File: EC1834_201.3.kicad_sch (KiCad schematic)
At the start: 64 parts

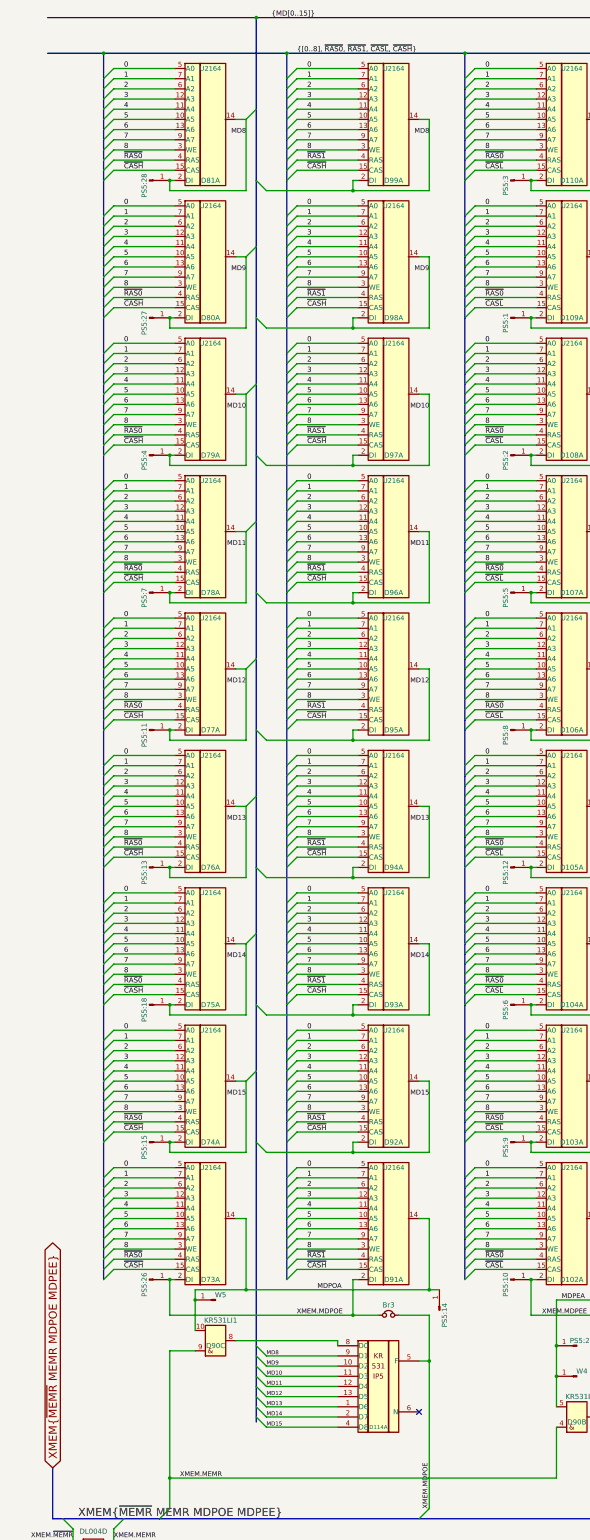
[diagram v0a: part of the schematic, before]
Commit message: Improved schematics and docs
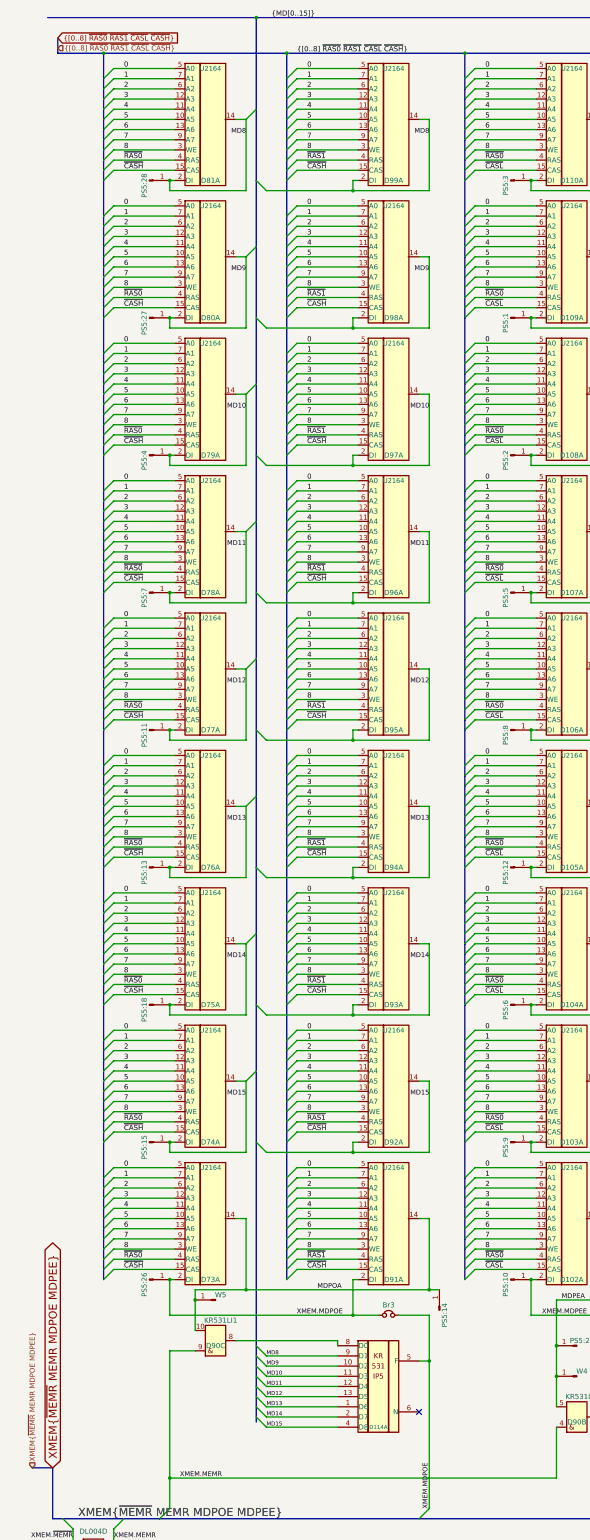
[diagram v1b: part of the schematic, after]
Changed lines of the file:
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@@
     (date "2022-09-05")
   )
+  (bus_alias "XMEM" (members ))
   (junction (at 144.78 231.14) (diameter 0) (color 0 0 0 0)
   )
@@
     (stroke (width 0) (type default) (color 0 0 0 0))
   )
+  (bus (pts (xy 26.67 24.13) (xy 26.67 27.94))
+    (stroke (width 0) (type default) (color 0 0 0 0))
+  )
   (wire (pts (xy 176.53 284.48) (xy 191.77 284.48))
     (stroke (width 0) (type default) (color 0 0 0 0))
@@
     (stroke (width 0) (type default) (color 0 0 0 0))
   )
+  (bus (pts (xy 20.32 381) (xy 25.4 381))
+    (stroke (width 0) (type default) (color 0 0 0 0))
+  )
   (bus (pts (xy 38.1 118.11) (xy 38.1 120.65))
     (stroke (width 0) (type default) (color 0 0 0 0))
@@
     (stroke (width 0) (type default) (color 0 0 0 0))
   )
-  (bus (pts (xy 38.1 27.94) (xy 24.13 27.94))
+  (bus (pts (xy 26.67 27.94) (xy 38.1 27.94))
     (stroke (width 0) (type default) (color 0 0 0 0))
   )
@@
     (effects (font (size 1.27 1.27)) (justify left bottom))
   )
-  (label "{[0..8], ~{RAS0}, ~{RAS1}, ~{CASL}, ~{CASH}}" (at 86.36 27.94 0)
+  (label "{[0..8] ~{RAS0} ~{RAS1} ~{CASL} ~{CASH}}" (at 86.36 27.94 0)
     (effects (font (size 1.27 1.27)) (justify left bottom))
   )
@@
     (effects (font (size 1.27 1.27)) (justify left bottom))
   )
+  (global_label "{[0..8] ~{RAS0} ~{RAS1} ~{CASL} ~{CASH}}" (shape input) (at 26.67 24.13 0) (fields_autoplaced)
+    (effects (font (size 1.27 1.27)) (justify left))
+    (property "Intersheet References" "${INTERSHEET_REFS}" (id 0) (at 58.9299 24.0506 0)
+      (effects (font (size 1.27 1.27)) (justify left) hide)
+    )
+  )
   (global_label "XMEM{~{MEMR} MEMR MDPOE MDPEE}" (shape bidirectional) (at 25.4 381 90) (fields_autoplaced)
     (effects (font (size 2.0066 2.0066)) (justify left))
@@
     )
   )
+  (hierarchical_label "XMEM{~{MEMR} MEMR MDPOE MDPEE}" (shape input) (at 20.32 381 90)
+    (effects (font (size 1.27 1.27)) (justify left))
+  )
+  (hierarchical_label "{[0..8] ~{RAS0} ~{RAS1} ~{CASL} ~{CASH}}" (shape input) (at 26.67 26.67 0)
+    (effects (font (size 1.27 1.27)) (justify left))
+  )
   (symbol (lib_id "robotron_ec1834:U2164") (at 64.77 80.01 0) (unit 1)

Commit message: Improved schematics
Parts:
- Br2, Br3: footprint (none) -> Resistor_THT:R_Axial_DIN0204_L3.6mm_D1.6mm_P7.62mm_Horizontal
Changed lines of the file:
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@@
       (effects (font (size 1.27 1.27)) hide)
     )
-    (property "Footprint" "" (id 2) (at 109.22 342.9 0)
+    (property "Footprint" "Resistor_THT:R_Axial_DIN0204_L3.6mm_D1.6mm_P7.62mm_Horizontal" (id 2) (at 109.22 342.9 0)
       (effects (font (size 1.27 1.27)) hide)
     )
@@
       (effects (font (size 1.27 1.27)) hide)
     )
-    (property "Footprint" "" (id 2) (at 199.39 342.9 0)
+    (property "Footprint" "Resistor_THT:R_Axial_DIN0204_L3.6mm_D1.6mm_P7.62mm_Horizontal" (id 2) (at 199.39 342.9 0)
       (effects (font (size 1.27 1.27)) hide)
     )

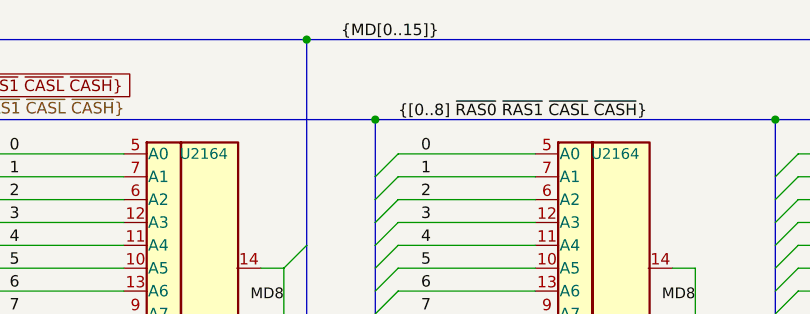
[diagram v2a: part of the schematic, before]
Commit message: corrected page names progress on page 2 added 1834 bus symbol
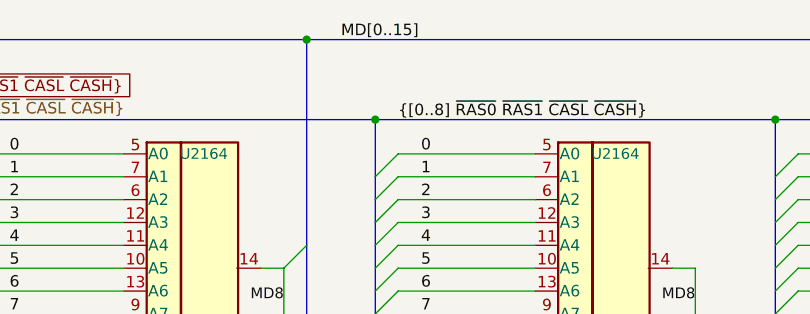
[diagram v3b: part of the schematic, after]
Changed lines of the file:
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@@
     (effects (font (size 1.27 1.27)) (justify left bottom))
   )
-  (label "{MD[0..15]}" (at 80.01 19.05 0)
+  (label "MD[0..15]" (at 80.01 19.05 0)
     (effects (font (size 1.27 1.27)) (justify left bottom))
   )

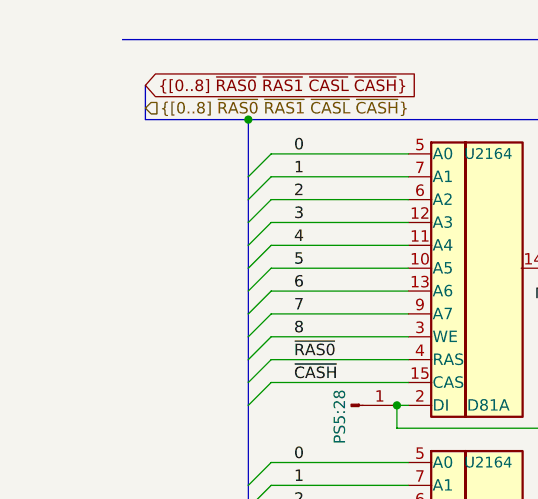
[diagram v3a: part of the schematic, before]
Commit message: Schematics almost done, need to connect busses
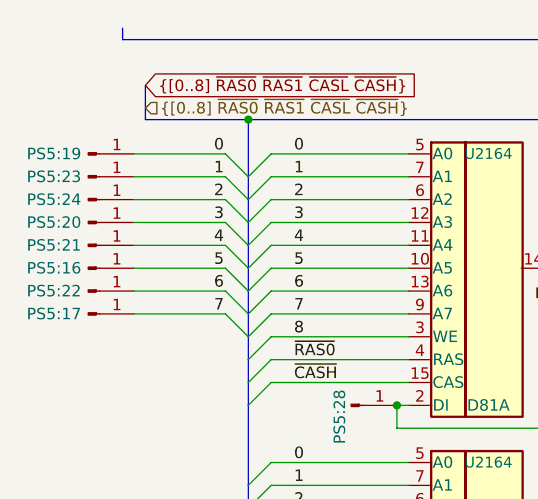
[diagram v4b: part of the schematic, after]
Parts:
- added PS5:16, PS5:17, PS5:19, PS5:20, PS5:21, PS5:22, PS5:23, PS5:24: PS5, symbol Connector:Conn_01x01_Male
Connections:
- net 0: now also PS5:19.1 (Pin_1)
- net 1: now also PS5:23.1 (Pin_1)
- net 2: now also PS5:24.1 (Pin_1)
- net 3: now also PS5:20.1 (Pin_1)
- net 4: now also PS5:21.1 (Pin_1)
- net 5: now also PS5:16.1 (Pin_1)
- net 6: now also PS5:22.1 (Pin_1)
- net 7: now also PS5:17.1 (Pin_1)

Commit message: Page 1 & 2 connected Hierarchival connections created and tested
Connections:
- net 0 renamed MEM0
- net 1 renamed MEM1
- net 2 renamed MEM2
- net 3 renamed MEM3
- net 4 renamed MEM4
- net 5 renamed MEM5
- net 6 renamed MEM6
- net 7 renamed MEM7
- net 8 renamed ~{WE}
- net XMEM.MDPEE renamed MDPEE
- net XMEM.MDPOE renamed MDPOE
- net XMEM.MEMR renamed MEMR
- net XMEM.~{MEMR} renamed ~{MEMR}

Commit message: Completed BUS Final checks required
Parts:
- D113, D114, D87, D90: footprint (none) -> Package_DIP:DIP-14_W7.62mm
- W4, W5: footprint (none) -> Connector_PinHeader_2.54mm:PinHeader_1x01_P2.54mm_Vertical
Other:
- company: (none) -> Mario Gögel 2022
- title: EC1834 201.3 RAM -> EC1834 Hauptplatine 201.2-RAM
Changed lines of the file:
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@@
   (paper "A3" portrait)
   (title_block
-    (title "EC1834 201.3 RAM")
-    (date "2022-09-05")
+    (title "EC1834 Hauptplatine 201.2-RAM")
+    (date "2022-09-12")
+    (rev "1")
+    (company "Mario Gögel 2022")
   )
   (bus_alias "XMEM" (members ))
@@
       (effects (font (size 1.27 1.27)) hide)
     )
-    (property "Footprint" "" (id 2) (at 106.68 361.95 0)
+    (property "Footprint" "Package_DIP:DIP-14_W7.62mm" (id 2) (at 106.68 361.95 0)
       (effects (font (size 1.27 1.27)) hide)
     )
@@
       (effects (font (size 1.27 1.27)) hide)
     )
-    (property "Footprint" "" (id 2) (at 198.12 359.41 0)
+    (property "Footprint" "Package_DIP:DIP-14_W7.62mm" (id 2) (at 198.12 359.41 0)
       (effects (font (size 1.27 1.27)) hide)
     )
@@
     (property "Reference" "D90" (id 0) (at 66.04 350.52 0))
     (property "Value" "KR531LI1" (id 1) (at 67.31 344.17 0))
-    (property "Footprint" "" (id 2) (at 66.04 349.25 0)
+    (property "Footprint" "Package_DIP:DIP-14_W7.62mm" (id 2) (at 66.04 349.25 0)
       (effects (font (size 1.27 1.27)) hide)
     )
@@
     (property "Reference" "D90" (id 0) (at 156.21 369.57 0))
     (property "Value" "KR531LI1" (id 1) (at 157.48 363.22 0))
-    (property "Footprint" "" (id 2) (at 156.21 368.3 0)
+    (property "Footprint" "Package_DIP:DIP-14_W7.62mm" (id 2) (at 156.21 368.3 0)
       (effects (font (size 1.27 1.27)) hide)
     )
@@
       (effects (font (size 1.27 1.27)) hide)
     )
-    (property "Footprint" "" (id 2) (at 156.21 358.14 0)
+    (property "Footprint" "Connector_PinHeader_2.54mm:PinHeader_1x01_P2.54mm_Vertical" (id 2) (at 156.21 358.14 0)
       (effects (font (size 1.27 1.27)) hide)
     )
@@
       (effects (font (size 1.27 1.27)) hide)
     )
-    (property "Footprint" "" (id 2) (at 66.04 339.09 0)
+    (property "Footprint" "Connector_PinHeader_2.54mm:PinHeader_1x01_P2.54mm_Vertical" (id 2) (at 66.04 339.09 0)
       (effects (font (size 1.27 1.27)) hide)
     )
@@
     (property "Reference" "D87" (id 0) (at 35.56 405.13 0))
     (property "Value" "DL004D" (id 1) (at 35.56 396.8496 0))
-    (property "Footprint" "" (id 2) (at 35.56 401.32 0)
+    (property "Footprint" "Package_DIP:DIP-14_W7.62mm" (id 2) (at 35.56 401.32 0)
       (effects (font (size 1.27 1.27)) hide)
     )

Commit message: Updated footprint for EMR UC8821 Added footprint for PS5 PCB layout in progress small corrections in schematics
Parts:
- PS5:1, PS5:10, PS5:11, PS5:12, PS5:13, PS5:14, PS5:15, PS5:16, PS5:17, PS5:18, PS5:19, PS5:2, PS5:20, PS5:21, PS5:22, PS5:23, PS5:24, PS5:25, PS5:26, PS5:27, PS5:28, PS5:3, PS5:4, PS5:5, PS5:6, PS5:7, PS5:8, PS5:9: footprint (none) -> EC1834-Board:Pruefstecker5_Single
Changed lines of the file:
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@@
       (effects (font (size 1.27 1.27)) hide)
     )
-    (property "Footprint" "" (id 2) (at 49.53 334.01 0)
+    (property "Footprint" "EC1834-Board:Pruefstecker5_Single" (id 2) (at 49.53 334.01 0)
       (effects (font (size 1.27 1.27)) hide)
     )
@@
       (effects (font (size 1.27 1.27)) hide)
     )
-    (property "Footprint" "" (id 2) (at 49.53 299.72 0)
+    (property "Footprint" "EC1834-Board:Pruefstecker5_Single" (id 2) (at 49.53 299.72 0)
       (effects (font (size 1.27 1.27)) hide)
     )
@@
       (effects (font (size 1.27 1.27)) hide)
     )
-    (property "Footprint" "" (id 2) (at 49.53 265.43 0)
+    (property "Footprint" "EC1834-Board:Pruefstecker5_Single" (id 2) (at 49.53 265.43 0)
       (effects (font (size 1.27 1.27)) hide)
     )
@@
       (effects (font (size 1.27 1.27)) hide)
     )
-    (property "Footprint" "" (id 2) (at 49.53 231.14 0)
+    (property "Footprint" "EC1834-Board:Pruefstecker5_Single" (id 2) (at 49.53 231.14 0)
       (effects (font (size 1.27 1.27)) hide)
     )
@@
       (effects (font (size 1.27 1.27)) hide)
     )
-    (property "Footprint" "" (id 2) (at 49.53 196.85 0)
+    (property "Footprint" "EC1834-Board:Pruefstecker5_Single" (id 2) (at 49.53 196.85 0)
       (effects (font (size 1.27 1.27)) hide)
     )
@@
       (effects (font (size 1.27 1.27)) hide)
     )
-    (property "Footprint" "" (id 2) (at 49.53 162.56 0)
+    (property "Footprint" "EC1834-Board:Pruefstecker5_Single" (id 2) (at 49.53 162.56 0)
       (effects (font (size 1.27 1.27)) hide)
     )
@@
       (effects (font (size 1.27 1.27)) hide)
     )
-    (property "Footprint" "" (id 2) (at 49.53 128.27 0)
+    (property "Footprint" "EC1834-Board:Pruefstecker5_Single" (id 2) (at 49.53 128.27 0)
       (effects (font (size 1.27 1.27)) hide)
     )
@@
       (effects (font (size 1.27 1.27)) hide)
     )
-    (property "Footprint" "" (id 2) (at 49.53 93.98 0)
+    (property "Footprint" "EC1834-Board:Pruefstecker5_Single" (id 2) (at 49.53 93.98 0)
       (effects (font (size 1.27 1.27)) hide)
     )
@@
       (effects (font (size 1.27 1.27)) hide)
     )
-    (property "Footprint" "" (id 2) (at 49.53 59.69 0)
+    (property "Footprint" "EC1834-Board:Pruefstecker5_Single" (id 2) (at 49.53 59.69 0)
       (effects (font (size 1.27 1.27)) hide)
     )
@@
       (effects (font (size 1.27 1.27)) hide)
     )
-    (property "Footprint" "" (id 2) (at 139.7 334.01 0)
+    (property "Footprint" "EC1834-Board:Pruefstecker5_Single" (id 2) (at 139.7 334.01 0)
       (effects (font (size 1.27 1.27)) hide)
     )
@@
       (effects (font (size 1.27 1.27)) hide)
     )
-    (property "Footprint" "" (id 2) (at 139.7 299.72 0)
+    (property "Footprint" "EC1834-Board:Pruefstecker5_Single" (id 2) (at 139.7 299.72 0)
       (effects (font (size 1.27 1.27)) hide)
     )
@@
       (effects (font (size 1.27 1.27)) hide)
     )
-    (property "Footprint" "" (id 2) (at 139.7 265.43 0)
+    (property "Footprint" "EC1834-Board:Pruefstecker5_Single" (id 2) (at 139.7 265.43 0)
       (effects (font (size 1.27 1.27)) hide)
     )
@@
       (effects (font (size 1.27 1.27)) hide)
     )
-    (property "Footprint" "" (id 2) (at 139.7 231.14 0)
+    (property "Footprint" "EC1834-Board:Pruefstecker5_Single" (id 2) (at 139.7 231.14 0)
       (effects (font (size 1.27 1.27)) hide)
     )
@@
       (effects (font (size 1.27 1.27)) hide)
     )
-    (property "Footprint" "" (id 2) (at 139.7 196.85 0)
+    (property "Footprint" "EC1834-Board:Pruefstecker5_Single" (id 2) (at 139.7 196.85 0)
       (effects (font (size 1.27 1.27)) hide)
     )
@@
       (effects (font (size 1.27 1.27)) hide)
     )
-    (property "Footprint" "" (id 2) (at 139.7 162.56 0)
+    (property "Footprint" "EC1834-Board:Pruefstecker5_Single" (id 2) (at 139.7 162.56 0)
       (effects (font (size 1.27 1.27)) hide)
     )
@@
       (effects (font (size 1.27 1.27)) hide)
     )
-    (property "Footprint" "" (id 2) (at 139.7 128.27 0)
+    (property "Footprint" "EC1834-Board:Pruefstecker5_Single" (id 2) (at 139.7 128.27 0)
       (effects (font (size 1.27 1.27)) hide)
     )
@@
       (effects (font (size 1.27 1.27)) hide)
     )
-    (property "Footprint" "" (id 2) (at 139.7 93.98 0)
+    (property "Footprint" "EC1834-Board:Pruefstecker5_Single" (id 2) (at 139.7 93.98 0)
       (effects (font (size 1.27 1.27)) hide)
     )
@@
       (effects (font (size 1.27 1.27)) hide)
     )
-    (property "Footprint" "" (id 2) (at 139.7 59.69 0)
+    (property "Footprint" "EC1834-Board:Pruefstecker5_Single" (id 2) (at 139.7 59.69 0)
       (effects (font (size 1.27 1.27)) hide)
     )
@@
       (effects (font (size 1.27 1.27)) hide)
     )
-    (property "Footprint" "" (id 2) (at 121.92 341.63 0)
+    (property "Footprint" "EC1834-Board:Pruefstecker5_Single" (id 2) (at 121.92 341.63 0)
       (effects (font (size 1.27 1.27)) hide)
     )
@@
       (effects (font (size 1.27 1.27)) hide)
     )
-    (property "Footprint" "" (id 2) (at 156.21 350.52 0)
+    (property "Footprint" "EC1834-Board:Pruefstecker5_Single" (id 2) (at 156.21 350.52 0)
       (effects (font (size 1.27 1.27)) hide)
     )
@@
       (effects (font (size 1.27 1.27)) hide)
     )
-    (property "Footprint" "" (id 2) (at 20.32 41.91 0)
+    (property "Footprint" "EC1834-Board:Pruefstecker5_Single" (id 2) (at 20.32 41.91 0)
       (effects (font (size 1.27 1.27)) hide)
     )
@@
       (effects (font (size 1.27 1.27)) hide)
     )
-    (property "Footprint" "" (id 2) (at 20.32 44.45 0)
+    (property "Footprint" "EC1834-Board:Pruefstecker5_Single" (id 2) (at 20.32 44.45 0)
       (effects (font (size 1.27 1.27)) hide)
     )
@@
       (effects (font (size 1.27 1.27)) hide)
     )
-    (property "Footprint" "" (id 2) (at 20.32 34.29 0)
+    (property "Footprint" "EC1834-Board:Pruefstecker5_Single" (id 2) (at 20.32 34.29 0)
       (effects (font (size 1.27 1.27)) hide)
     )
@@
       (effects (font (size 1.27 1.27)) hide)
     )
-    (property "Footprint" "" (id 2) (at 20.32 31.75 0)
+    (property "Footprint" "EC1834-Board:Pruefstecker5_Single" (id 2) (at 20.32 31.75 0)
       (effects (font (size 1.27 1.27)) hide)
     )
@@
       (effects (font (size 1.27 1.27)) hide)
     )
-    (property "Footprint" "" (id 2) (at 20.32 36.83 0)
+    (property "Footprint" "EC1834-Board:Pruefstecker5_Single" (id 2) (at 20.32 36.83 0)
       (effects (font (size 1.27 1.27)) hide)
     )
@@
       (effects (font (size 1.27 1.27)) hide)
     )
-    (property "Footprint" "" (id 2) (at 20.32 46.99 0)
+    (property "Footprint" "EC1834-Board:Pruefstecker5_Single" (id 2) (at 20.32 46.99 0)
       (effects (font (size 1.27 1.27)) hide)
     )
@@
       (effects (font (size 1.27 1.27)) hide)
     )
-    (property "Footprint" "" (id 2) (at 20.32 49.53 0)
+    (property "Footprint" "EC1834-Board:Pruefstecker5_Single" (id 2) (at 20.32 49.53 0)
       (effects (font (size 1.27 1.27)) hide)
     )
@@
       (effects (font (size 1.27 1.27)) hide)
     )
-    (property "Footprint" "" (id 2) (at 20.32 39.37 0)
-      (effects (font (size 1.27 1.27)) hide)
-    )
+    (property "Footprint" "EC1834-Board:Pruefstecker5_Single" (id 2) (at 20.32 39.37 0)
+      (effects (font (size 1.27 1.27)) hide)
+    )

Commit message: Completed PCB layout Changed PS5
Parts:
- removed PS5:1, PS5:10, PS5:11, PS5:12, PS5:13, PS5:14, PS5:15, PS5:16, PS5:17, PS5:18, PS5:19, PS5:2, PS5:20, PS5:21, PS5:22, PS5:23, PS5:24, PS5:25, PS5:26, PS5:27, PS5:28, PS5:3, PS5:4, PS5:5, PS5:6, PS5:7, PS5:8, PS5:9: PS5, EC1834-Board:Pruefstecker5_Single, symbol Connector:Conn_01x01_Male
- added PS5: PS5, EC1834-Board:Pruefstecker5, symbol Connector_Generic:Conn_01x28
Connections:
- net MD0: now also PS5.3 (Pin_3)
- net MD1: now also PS5.1 (Pin_1)
- net MD10: now also PS5.4 (Pin_4)
- net MD11: now also PS5.7 (Pin_7)
- net MD12: now also PS5.11 (Pin_11)
- net MD13: now also PS5.13 (Pin_13)
- net MD14: now also PS5.18 (Pin_18)
- net MD15: now also PS5.15 (Pin_15)
- net MD2: now also PS5.2 (Pin_2)
- net MD3: now also PS5.5 (Pin_5)
- net MD4: now also PS5.8 (Pin_8)
- net MD5: now also PS5.12 (Pin_12)
- net MD6: now also PS5.6 (Pin_6)
- net MD7: now also PS5.9 (Pin_9)
- net MD8: now also PS5.28 (Pin_28)
- net MD9: now also PS5.27 (Pin_27)
- net MDPEA: now also PS5.25 (Pin_25)
- net MDPEE: now also PS5.10 (Pin_10)
- net MDPOA: now also PS5.14 (Pin_14)
- net MDPOE: now also PS5.26 (Pin_26)
- net MEM0: now also PS5.19 (Pin_19)
- net MEM1: now also PS5.23 (Pin_23)
- net MEM2: now also PS5.24 (Pin_24)
- net MEM3: now also PS5.20 (Pin_20)
- net MEM4: now also PS5.21 (Pin_21)
- net MEM5: now also PS5.16 (Pin_16)
- net MEM6: now also PS5.22 (Pin_22)
- net MEM7: now also PS5.17 (Pin_17)
